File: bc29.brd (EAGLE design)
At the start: 160 x 100 mm, 67 parts, among them IC1 LP2951D, IC10 TLC27L41, IC11 4001D, IC2 HCF4520, IC3 4053D, IC4 4093D, IC5 4013D, IC6 4013D, IC8 Teledyne TSC900BIJA, IC9 4060D, Q1 IRF740, X1 32KHz, X2 2520-5

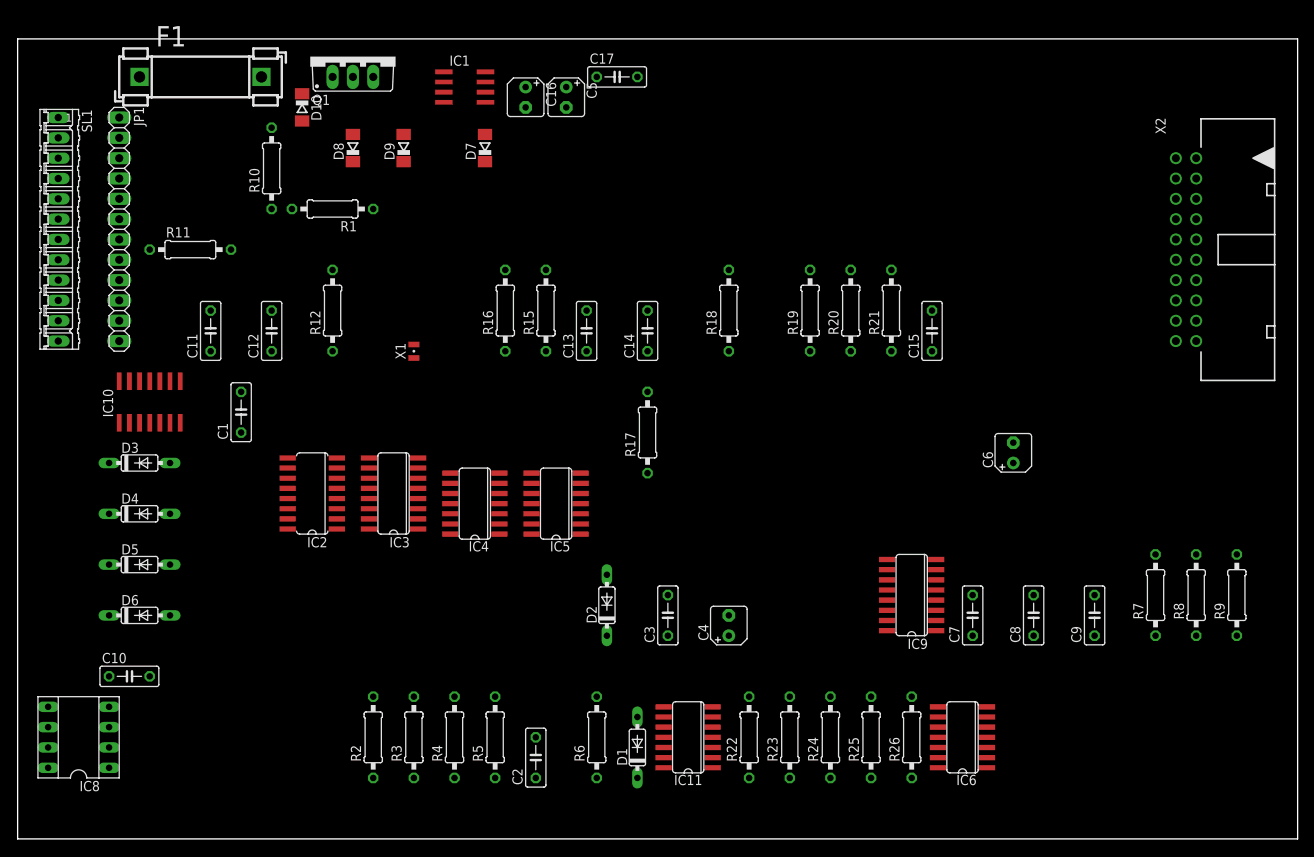
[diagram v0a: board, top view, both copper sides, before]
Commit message: Complete board silk screen. Update schematic to match
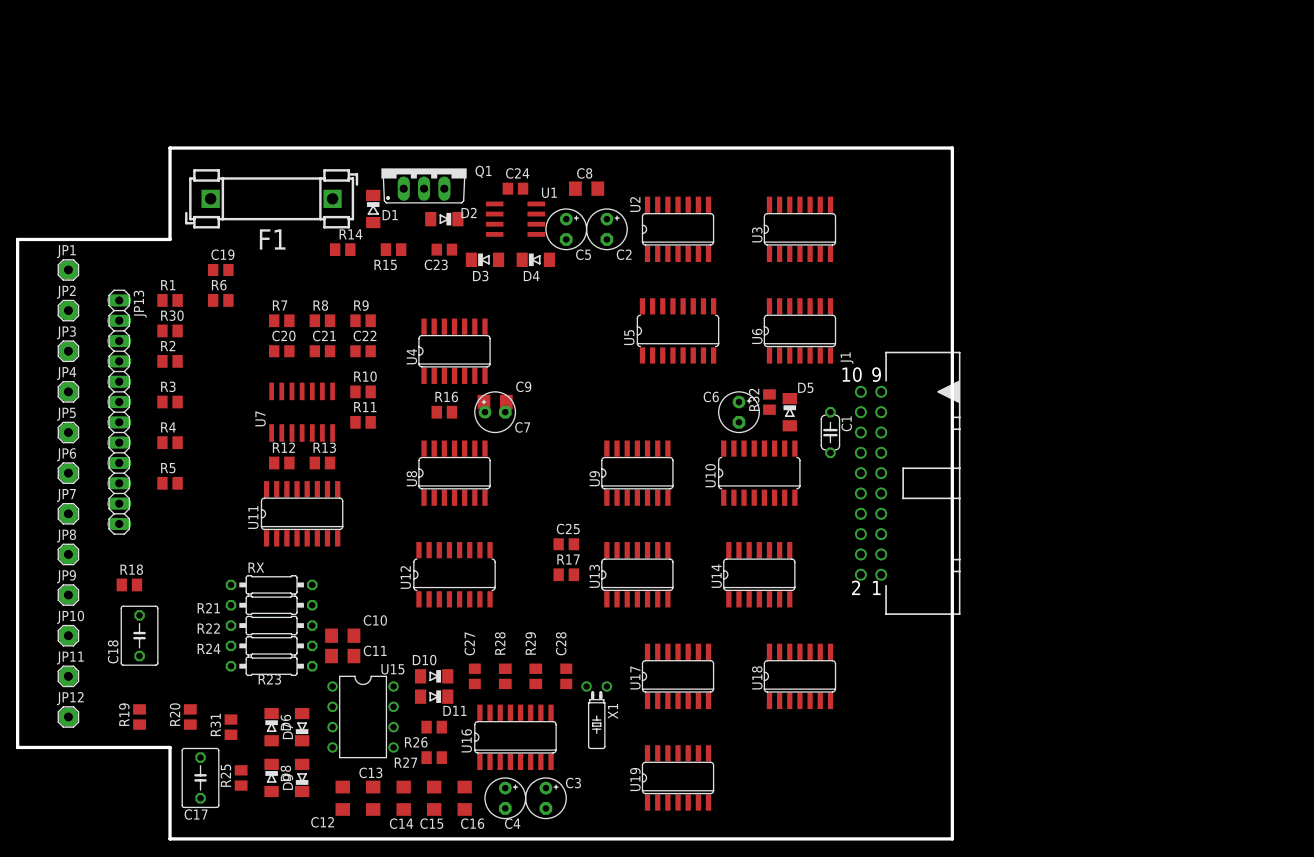
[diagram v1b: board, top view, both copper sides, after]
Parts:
- removed IC1: LP2951D, linear:SO08
- removed IC10: TLC27L41, linear:SO14
- removed IC11: 4001D, 40xx:SO14
- removed IC2: HCF4520, 45xx:SO16
- removed IC3: 4053D, 40xx:SO16
- removed IC4: 4093D, 40xx:SO14
- removed IC5, IC6: 4013D, 40xx:SO14
- removed IC8: Teledyne TSC900BIJA, ic-package:SOCKET-08
- removed IC9: 4060D, 40xx:SO16
- removed SL1: (no value), con-amp-quick:12P
- removed X2: 2520-5, con-3m:PAK100/2500-5-20
- added C18: (no value), rcl:C050-045X075
- added C19, C20, C21, C22, C23, C24, C25, C27, C28: (no value), rcl:C0805
- added D11: 1n4148, diode:MINIMELF
- added J1: 2520-5, con-3m:PAK100/2500-5-20
- added JP10, JP11, JP12, JP2, JP3, JP4, JP5, JP6, JP7, JP8, JP9: (no value), pinhead:1X01
- added JP13: (no value), pinhead:1X12
- added R13: 3K, rcl:M0805
- added R14: 1M, rcl:M0805
- added R27: 47, rcl:M0805
- added R28: 10M, rcl:M0805
- added R29: 330K, rcl:M0805
- added R30, R32: 1K, rcl:M0805
- added R31: 10K, rcl:M0805
- added RX: OPEN, rcl:0207/10
- added U1: LP2951, linear:SO08
- added U10, U5: MC14516B, 45xx:SO16
- added U11: CD4053B, 40xx:SO16
- added U12: HCF4520, 45xx:SO16
- added U13, U8: CD4013B, 40xx:SO14
- added U14, U18: CD4070B, 40xx:SO14
- added U15: TSC900BIJA, linear:DIL08
- added U16: CD4060B, 40xx:SO16
- added U17: MC14073B, 40xx:SO14
- added U19, U9: CD4001B, 40xx:SO14
- added U2: CD4081, 40xx:SO14
- added U3: CD4023, 40xx:SO14
- added U4: CD4093B, 40xx:SO14
- added U6: CD4013, 40xx:SO14
- added U7: TLC27L41, linear:SO14
- C1: device rcl:C050-025X075 -> rcl:C050-024X044
- C10, C11: value Poly -> (none); device rcl:C050-025X075 -> rcl:C1206
- C12, C13, C14, C15, C8, C9: device rcl:C050-025X075 -> rcl:C1206
- C16: value 10uF 63V -> (none); device rcl:B45181A -> rcl:C1206
- C17: device rcl:C050-025X075 -> rcl:C050-045X075
- C2, C3: value (none) -> 47uf 25V; device rcl:C050-025X075 -> rcl:E2,5-5
- C4: value 47uF 25V -> 47uf 25V; device rcl:B45181A -> rcl:E2,5-5
- C5, C6: value 47uF 25V -> 10uF 63V; device rcl:B45181A -> rcl:E2,5-5
- C7: value (none) -> 10uF 63V; device rcl:C050-025X075 -> rcl:E2,5-5
- D1: value 1N4148 -> V674; device diode:DO35-7 -> diode:SOD80C
- D10, D8, D9: value (none) -> 1n4148; device diode:SOD80C -> diode:MINIMELF
- D2, D4: device diode:DO35-7 -> diode:MINIMELF
- D3, D5: value 1N4148 -> ZENER?; device diode:DO35-7 -> diode:MINIMELF
- D6: value 1N4148 -> 1n4148; device diode:DO35-7 -> diode:MINIMELF
- D7: value (none) -> 1N4148; device diode:SOD80C -> diode:MINIMELF
- JP1: device pinhead:1X12 -> pinhead:1X01
- R1: value 1M -> 20K; device rcl:0207/10 -> rcl:M0805
- R10: device rcl:0207/10 -> rcl:M0805
- R11: value (none) -> 1M; device rcl:0207/10 -> rcl:M0805
- R12: value 3K -> 1M; device rcl:0207/10 -> rcl:M0805
- R15: value 10M -> 1M; device rcl:0207/10 -> rcl:M0805
- R16: value 330K -> 100K; device rcl:0207/10 -> rcl:M0805
- R17: value 1M -> 100K; device rcl:0207/10 -> rcl:M0805
- R18: value 1M -> 300; device rcl:0207/10 -> rcl:M0805
- R19: value 330K -> 300; device rcl:0207/10 -> rcl:M0805
- R2: value 300 -> 20K; device rcl:0207/10 -> rcl:M0805
- R20: value 330K -> 2K; device rcl:0207/10 -> rcl:M0805
- R21: value 330K -> 130K
- R22: value 2K -> 130K
- R23: value 2K -> 4.70K
- R24: value 2K -> 8.20K
- R25: value 20K -> 620; device rcl:0207/10 -> rcl:M0805
- R26: value 1K -> 47; device rcl:0207/10 -> rcl:M0805
- R3: value 620 -> 2K; device rcl:0207/10 -> rcl:M0805
- R4: value 300 -> 2K; device rcl:0207/10 -> rcl:M0805
- R5: value 47 -> 2K; device rcl:0207/10 -> rcl:M0805
- R6: value 47 -> 100K; device rcl:0207/10 -> rcl:M0805
- R7, R8: value 130K -> 330K; device rcl:0207/10 -> rcl:M0805
- R9: value 110K -> 330K; device rcl:0207/10 -> rcl:M0805
- X1: value 32KHz -> 32.768KHz; device crystal:FC-12M -> crystal:TC26H
- moved R7 114.5 mm to (33.0, 64.8), turned to 0 degrees
- moved R8 114.5 mm to (38.1, 64.8), turned to 0 degrees
- moved R9 114.5 mm to (43.2, 64.8), turned to 0 degrees
- moved C17 101.9 mm to (22.9, 7.62), turned to 90 degrees
- moved R19 98.0 mm to (15.2, 15.2)
- moved R20 96.9 mm to (21.6, 15.2)
- moved C16 88.0 mm to (55.9, 5.08), turned to 90 degrees
- moved R21 85.8 mm to (31.8, 29.2), turned to 0 degrees
- moved C15 85.4 mm to (52.1, 5.08)
- moved D5 83.5 mm to (96.5, 53.3), turned to 270 degrees
- moved R18 82.4 mm to (14.0, 31.8), turned to 0 degrees
- moved D9 79.8 mm to (35.6, 7.62)
- moved C9 79.5 mm to (59.7, 54.6), turned to 0 degrees
- moved D8 79.4 mm to (31.8, 7.62), turned to 270 degrees
- moved R25 78.9 mm to (27.9, 7.62)
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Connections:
- removed net +12V: D9.A, IC10.4, IC3.15, R18.1, R5.2
- removed net 12V+: JP1.11, SL1.11, X2.4
- removed net 12V-: JP1.12, SL1.12, X2.2
- removed net 2KHZ: C6.+, IC9.7
- removed net 32_47KHZ: IC9.9
- removed net N$1: D10.A, F1.2, R10.2
- removed net N$10: C3.1, IC8.4, R6.1
- removed net N$11: C7.2, IC8.1
- removed net N$12: C8.2, C9.2, IC10.2, IC8.6
- removed net N$2: R1.2, R10.1
- removed net N$3: C10.1, D5.A, D6.C, IC8.3, R3.1
- removed net N$4: C11.1, R2.2, R4.1
- removed net N$5: C12.1, C8.1, C9.1, D3.C, D4.A, IC8.2, R11.2, R4.2, R7.2
- removed net N$6: C1.2, IC8.8
- removed net N$7: C2.2, IC8.7, R5.1
- removed net N$8: C12.2, IC3.2, R8.2
- removed net N$9: C6.-, D1.C, D2.A
- new net -1V25: C20.2, C21.1, R7.2, R8.1, U7.9
- new net 0V0: C21.2, R8.2, R9.1, U7.13
- new net 12+: J1.4, JP11.1, JP13.11
- new net 12-: J1.2, JP12.1, JP13.12
- new net 13V5: C5.+, D2.A, Q1.S, U1.8
- new net 1V25: C22.2, R12.1, R9.2, U7.3
- new net 1_024KHZ: U16.5
- new net 1_031KHZ: U8.11, U8.3
- new net 2_048KHZ: C3.+, U16.7
- new net 32_768KHZ: R28.1, R29.1, U16.10
- new net 4HZ: U12.2, U16.2
- new net DRAIN: D1.C, Q1.D
- new net FUSED_BATT+: D1.A, F1.2, R14.2
- new net GATE: C23.1, D2.C, D3.C, Q1.G, R15.2
- new net LCD-20: C6.-, D5.C, J1.20
- new net N$14: J1.10, U14.10
- new net N$16: J1.8, U14.4
- new net N$39: C27.2, R29.2, X1.1
- new net N$40: C28.2, R28.2, U16.11, X1.2
- new net N$41: C13.1, U15.1
- new net N$42: R21.1, R22.2
- new net N$43: C14.1, U15.8
- new net N$44: U1.6, U1.7
- new net N$45: R23.1, R24.2
- new net N$46: R13.1, U11.14
- new net N$47: R13.2, U7.6, U7.7
- new net N$48: R16.1, U4.10
- new net N$49: R17.2, U13.6
- new net N$51: C19.1, R1.2, R6.1
- new net N$52: U10.15, U5.15
- new net N$53: R11.2, U8.5
- new net N$54: C6.+, R32.1
- new net N$55: R10.1, U7.8
- new net N$56: R11.1, U7.1
- new net N$57: R10.2, U8.9
- new net N$60: U19.8, U9.2
- new net RESET_R: C7.+, C9.1, R16.2, R2.2, U4.5, U4.6
- new net U8-1: U11.10, U8.1, U9.1
- new net U8-13: U11.11, U8.13
- new net U8-SET: C25.1, R17.1, U4.12, U8.6, U8.8
- net !RESET: now also U4.4; no longer IC3.9, IC4.4, IC5.4, IC6.10
- net +5V: now also C2.+, C24.1, C8.1, D3.A, D4.C, J1.14, R12.2, R26.2, U1.1, U1.2, U11.15, U11.5, U4.13, U7.4; no longer C15.2, C4.+, D8.C, IC1.1, IC1.2
- net +BATT: now also JP13.1; no longer SL1.1
- net -2V5: now also C20.1, R7.1, U7.14, U7.5; no longer IC10.5
- net -4V: now also C4.-, D11.A; no longer C5.-, D1.A, IC10.11
- net -5V: now also C16.1, R27.1, U7.11; no longer R6.2
- net AH_NEGATIVE: now also JP13.8, JP8.1, R3.1; no longer JP1.8, R23.1, SL1.8
- net GND: now also C1.2, C12.2, C13.2, C14.2, C15.2, C16.2, C17.2, C18.2, C19.2, C2.-, C22.1, C23.2, C24.2, C27.1, C28.1, C4.+, C5.-, C7.-, C8.2, C9.2, D10.C, D4.A, D7.C, D9.C, J1.5, JP13.2, JP2.1, R30.2, U1.4, U11.3, U11.6, U11.8, U16.12, U7.12, U8.10, U8.4; no longer C1.1, C10.2, C11.2, C13.1, C14.1, C16.-, C17.1, C2.1, C3.2, C4.-, C5.+, C7.1, D2.C, D3.A, D4.C, D5.C, IC1.4, IC3.6, IC3.8, IC9.12, JP1.2, R26.2, SL1.2, X2.3
- net GND1K: now also JP13.6, JP6.1, R30.1; no longer JP1.6, R26.1, SL1.6
- net N$13: now also C1.1, J1.3, U2.4; no longer IC3.12, R9.2
- net N$15: now also J1.1, U18.10; no longer C13.2, IC9.11, R15.1, X1.2
- net N$17: now also J1.7, U14.11; no longer R11.1, R9.1
- net N$18: now also J1.9, U17.10, U5.5; no longer R7.1, R8.1
- net N$19: now also J1.11, U14.3; no longer IC10.6, IC10.7, R12.2
- net N$20: now also J1.13, U3.9; no longer IC3.14, R12.1
- net N$21: now also J1.15, U18.3, U3.11; no longer C14.2, R16.1, X1.1
- net N$22: now also J1.17, U11.4; no longer IC9.10, R15.2, R16.2
- net N$23: now also J1.19, U14.12, U14.2, U14.5, U14.9; no longer IC10.3, R18.2, R19.2
- net N$24: now also C25.2, U19.10; no longer IC10.1, R17.2
- net N$25: now also D5.A, U10.12; no longer R19.1, R20.2
- net N$26: now also J1.18, U18.9, U4.9; no longer R20.1, R21.2
- net N$27: now also C18.1, R18.2, R19.1; no longer IC2.2, IC9.2
- net N$28: now also J1.16, U19.3; no longer IC10.14, R21.1
- net N$29: now also R14.1, R15.1; no longer D10.C, Q1.D
- net N$30: now also C10.1, C11.1, D6.C, D7.A, R19.2, R20.1, R21.2, R23.2, R31.1, RX.2, U15.2; no longer C15.1, IC1.7
- net N$31: now also C15.1, R26.1, U15.7; no longer IC3.11, IC5.13
- net N$32: now also R32.2, U5.2; no longer IC10.12, IC3.3
- net N$33: now also C12.1, R27.2, U15.4; no longer IC11.1, IC3.10, IC5.1
- net N$34: now also C10.2, C11.2, U15.6, U7.10, U7.2; no longer IC3.4
- net N$35: now also R20.2, R24.1, RX.1, U11.12; no longer IC5.5, R17.1
- net N$36: now also C17.1, D8.C, D9.A, U15.3; no longer IC4.5, IC4.6
- net N$37: now also R22.1, R31.2, U11.2; no longer C17.2, D7.C, D9.C, Q1.G, R1.1
- net N$38: now also C3.-, D10.A, D11.C; no longer C16.+, D7.A, IC1.8, Q1.S
- net NAR: now also JP13.5, JP5.1, R1.1; no longer JP1.5, SL1.5
- net OUT+: now also JP13.9, JP9.1, R4.1; no longer JP1.9, R24.1, SL1.9
- net OUT-: now also JP10.1, JP13.10, R5.1; no longer JP1.10, R22.1, SL1.10
- net RESET: now also JP13.7, JP7.1, R2.1; no longer JP1.7, R25.1, SL1.7
- net SHUNT+: now also JP13.4, JP4.1, R18.1; no longer JP1.4, R2.1, SL1.4
- net SHUNT-: now also JP13.3, JP3.1, R25.1; no longer JP1.3, R3.2, SL1.3
- net VCC: now also U11.16; no longer IC3.16
- net VDD: now also U10.16, U12.16, U13.14, U14.14, U16.16, U17.14, U18.14, U19.14, U2.14, U3.14, U4.14, U5.16, U6.14, U8.14, U9.14; no longer IC11.14, IC2.16, IC4.14, IC5.14, IC6.14, IC9.16
- net VEE: now also U11.7; no longer IC3.7
- net VSS: now also U10.8, U12.8, U13.7, U14.7, U16.8, U17.7, U18.7, U19.7, U2.7, U3.7, U4.7, U5.8, U6.7, U8.7, U9.7; no longer IC11.7, IC2.8, IC4.7, IC5.7, IC6.7, IC9.8
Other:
- board size 160 x 100 mm -> 116.8 x 86.4 mm
- board text added: "1"
- board text added: "10"
- board text added: "2"
- board text added: "9"

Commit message: Charge/discharge output
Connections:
- net NAR renamed !NAR
- net U8-1 renamed CHARGE
- removed net 1_031KHZ: U8.11, U8.3
- removed net U8-13: U11.11, U8.13
- new net DISCHAR: U11.11, U8.13, U9.13
- new net N$50: R5.2, U2.3
- new net N$58: R4.2, U2.11
- new net N$59: U2.2, U9.11
- new net N$61: U2.12, U9.3
- new net U13-1: R3.2, R6.2, U13.1
- net !RESET: now also JP13.7, JP7.1, R2.1; no longer U4.4
- net +5V: now also U2.1, U2.13
- net 1_024KHZ: now also U8.11, U8.3
- net RESET: now also U4.4; no longer JP13.7, JP7.1, R2.1
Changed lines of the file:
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@@
 <contactref element="C24" pad="2"/>
 <contactref element="C8" pad="2"/>
-<contactref element="C23" pad="2"/>
 <contactref element="U16" pad="12"/>
 <contactref element="C4" pad="+"/>
@@
 <contactref element="C22" pad="1"/>
 <contactref element="R30" pad="2"/>
-<contactref element="C19" pad="2"/>
 <contactref element="U8" pad="4"/>
 <contactref element="U8" pad="10"/>
 <contactref element="C7" pad="-"/>
 <contactref element="C9" pad="2"/>
+<contactref element="C23" pad="2"/>
+<contactref element="C19" pad="2"/>
 <wire x1="101.6" y1="48.26" x2="105.41" y2="50.8" width="0" layer="19" extent="1-1"/>
 <wire x1="73.66" y1="74.93" x2="101.6" y2="48.26" width="0" layer="19" extent="1-1"/>
@@
 <wire x1="13.02" y1="31.75" x2="6.35" y2="55.88" width="0" layer="19" extent="1-1"/>
 </signal>
-<signal name="NAR">
+<signal name="!NAR">
 <contactref element="JP5" pad="1"/>
 <contactref element="JP13" pad="5"/>
@@
 </signal>
 <signal name="RESET">
-<contactref element="JP7" pad="1"/>
-<contactref element="JP13" pad="7"/>
-<contactref element="R2" pad="1"/>
-<wire x1="12.7" y1="52.07" x2="18.1" y2="59.69" width="0" layer="19" extent="1-1"/>
-<wire x1="6.35" y1="40.64" x2="12.7" y2="52.07" width="0" layer="19" extent="1-1"/>
+<contactref element="U4" pad="4"/>
 </signal>
 <signal name="AH_NEGATIVE">
@@
 <contactref element="R12" pad="2"/>
 <contactref element="U4" pad="13"/>
+<contactref element="U2" pad="1"/>
+<contactref element="U2" pad="13"/>
+<wire x1="78.74" y1="73.1266" x2="80.01" y2="79.2734" width="0" layer="19" extent="1-1"/>
+<wire x1="73.66" y1="77.47" x2="80.01" y2="79.2734" width="0" layer="19" extent="1-1"/>
 <wire x1="69.72" y1="81.28" x2="73.66" y2="77.47" width="0" layer="19" extent="1-1"/>
 <wire x1="61.28" y1="81.28" x2="69.72" y2="81.28" width="0" layer="19" extent="1-1"/>
@@
 <wire x1="36.195" y1="37.5666" x2="32.385" y2="43.7134" width="0" layer="19" extent="1-1"/>
 <wire x1="53.02" y1="13.97" x2="36.195" y2="37.5666" width="0" layer="19" extent="1-1"/>
-<wire x1="107.95" y1="40.64" x2="73.66" y2="77.47" width="0" layer="19" extent="1-1"/>
+<wire x1="107.95" y1="40.64" x2="78.74" y2="73.1266" width="0" layer="19" extent="1-1"/>
 </signal>
 <signal name="N$19">
@@
 <contactref element="U12" pad="2"/>
 <wire x1="59.055" y1="9.6266" x2="51.435" y2="29.9466" width="0" layer="19" extent="1-1"/>
-</signal>
-<signal name="1_031KHZ">
-<contactref element="U8" pad="11"/>
-<contactref element="U8" pad="3"/>
-<wire x1="53.34" y1="42.6466" x2="54.61" y2="48.7934" width="0" layer="19" extent="1-1"/>
 </signal>
 <signal name="N$36">
@@
 <wire x1="20" y1="67.31" x2="24.45" y2="67.31" width="0" layer="19" extent="1-1"/>
 </signal>
-<signal name="!RESET">
-<contactref element="U4" pad="4"/>
-</signal>
 <signal name="RESET_R">
 <contactref element="R2" pad="2"/>
@@
 <wire x1="86.36" y1="10.6934" x2="74.93" y2="42.6466" width="0" layer="19" extent="1-1"/>
 </signal>
-<signal name="U8-13">
-<contactref element="U8" pad="13"/>
-<contactref element="U11" pad="11"/>
-<wire x1="37.465" y1="43.7134" x2="52.07" y2="48.7934" width="0" layer="19" extent="1-1"/>
-</signal>
-<signal name="U8-1">
-<contactref element="U8" pad="1"/>
-<contactref element="U9" pad="1"/>
-<contactref element="U11" pad="10"/>
-<wire x1="50.8" y1="42.6466" x2="73.66" y2="42.6466" width="0" layer="19" extent="1-1"/>
-<wire x1="38.735" y1="43.7134" x2="50.8" y2="42.6466" width="0" layer="19" extent="1-1"/>
-</signal>
 <signal name="1V25">
 <contactref element="C22" pad="2"/>
@@
 <signal name="1_024KHZ">
 <contactref element="U16" pad="5"/>
+<contactref element="U8" pad="11"/>
+<contactref element="U8" pad="3"/>
+<wire x1="53.34" y1="42.6466" x2="54.61" y2="48.7934" width="0" layer="19" extent="1-1"/>
+<wire x1="62.865" y1="9.6266" x2="53.34" y2="42.6466" width="0" layer="19" extent="1-1"/>
 </signal>
 <signal name="N$32">
@@
 <wire x1="83.82" y1="10.6934" x2="69.53" y2="36.83" width="0" layer="19" extent="1-1"/>
 </signal>
+<signal name="!RESET">
+<contactref element="JP13" pad="7"/>
+<contactref element="JP7" pad="1"/>
+<contactref element="R2" pad="1"/>
+<wire x1="12.7" y1="52.07" x2="18.1" y2="59.69" width="0" layer="19" extent="1-1"/>
+<wire x1="6.35" y1="40.64" x2="12.7" y2="52.07" width="0" layer="19" extent="1-1"/>
+</signal>
+<signal name="U13-1">
+<contactref element="U13" pad="1"/>
+<contactref element="R6" pad="2"/>
+<contactref element="R3" pad="2"/>
+<wire x1="20" y1="54.61" x2="73.66" y2="29.9466" width="0" layer="19" extent="1-1"/>
+<wire x1="26.35" y1="67.31" x2="20" y2="54.61" width="0" layer="19" extent="1-1"/>
+</signal>
+<signal name="N$50">
+<contactref element="R5" pad="2"/>
+<contactref element="U2" pad="3"/>
+<wire x1="20" y1="44.45" x2="81.28" y2="73.1266" width="0" layer="19" extent="1-1"/>
+</signal>
+<signal name="N$58">
+<contactref element="R4" pad="2"/>
+<contactref element="U2" pad="11"/>
+<wire x1="20" y1="49.53" x2="82.55" y2="79.2734" width="0" layer="19" extent="1-1"/>
+</signal>
+<signal name="N$59">
+<contactref element="U2" pad="2"/>
+<contactref element="U9" pad="11"/>
+<wire x1="77.47" y1="48.7934" x2="80.01" y2="73.1266" width="0" layer="19" extent="1-1"/>
+</signal>
+<signal name="N$61">
+<contactref element="U2" pad="12"/>
+<contactref element="U9" pad="3"/>
+<wire x1="76.2" y1="42.6466" x2="81.28" y2="79.2734" width="0" layer="19" extent="1-1"/>
+</signal>
+<signal name="DISCHAR">
+<contactref element="U8" pad="13"/>
+<contactref element="U11" pad="11"/>
+<contactref element="U9" pad="13"/>
+<wire x1="52.07" y1="48.7934" x2="74.93" y2="48.7934" width="0" layer="19" extent="1-1"/>
+<wire x1="37.465" y1="43.7134" x2="52.07" y2="48.7934" width="0" layer="19" extent="1-1"/>
+</signal>
+<signal name="CHARGE">
+<contactref element="U8" pad="1"/>
+<contactref element="U9" pad="1"/>
+<contactref element="U11" pad="10"/>
+<wire x1="50.8" y1="42.6466" x2="73.66" y2="42.6466" width="0" layer="19" extent="1-1"/>
+<wire x1="38.735" y1="43.7134" x2="50.8" y2="42.6466" width="0" layer="19" extent="1-1"/>
+</signal>
 </signals>
